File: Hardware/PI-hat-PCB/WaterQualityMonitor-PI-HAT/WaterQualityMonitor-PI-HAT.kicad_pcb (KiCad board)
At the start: 2 copper layers, 65 x 106.7 mm, 84 parts, among them IC1 P82B96TD,118, IC2 DMMT5401-7-F, J1 Screw_Terminal_01x04, J10 GPIO, J2 Screw_Terminal_01x04, J3 Screw_Terminal_01x04, J4 Screw_Terminal_01x02, J5 Jack-DC 12V+, J6 SM04B-SRSS-TB(LF)(SN), M1 Fan, Q1 IRL540SPBF, Q2 IRL540SPBF, Q3 DMG2305UX-7, U1 DRV8870DDA, U2 TPS61169DCKR, U3 TMC2208_SILENTSTEPSTICK, U4 TMC2208_SILENTSTEPSTICK, U5 RT7272AGSP, U6 TMC2208_SILENTSTEPSTICK, U7 DRV8838, U8 RT7272AGSP, U9 CAT24C256

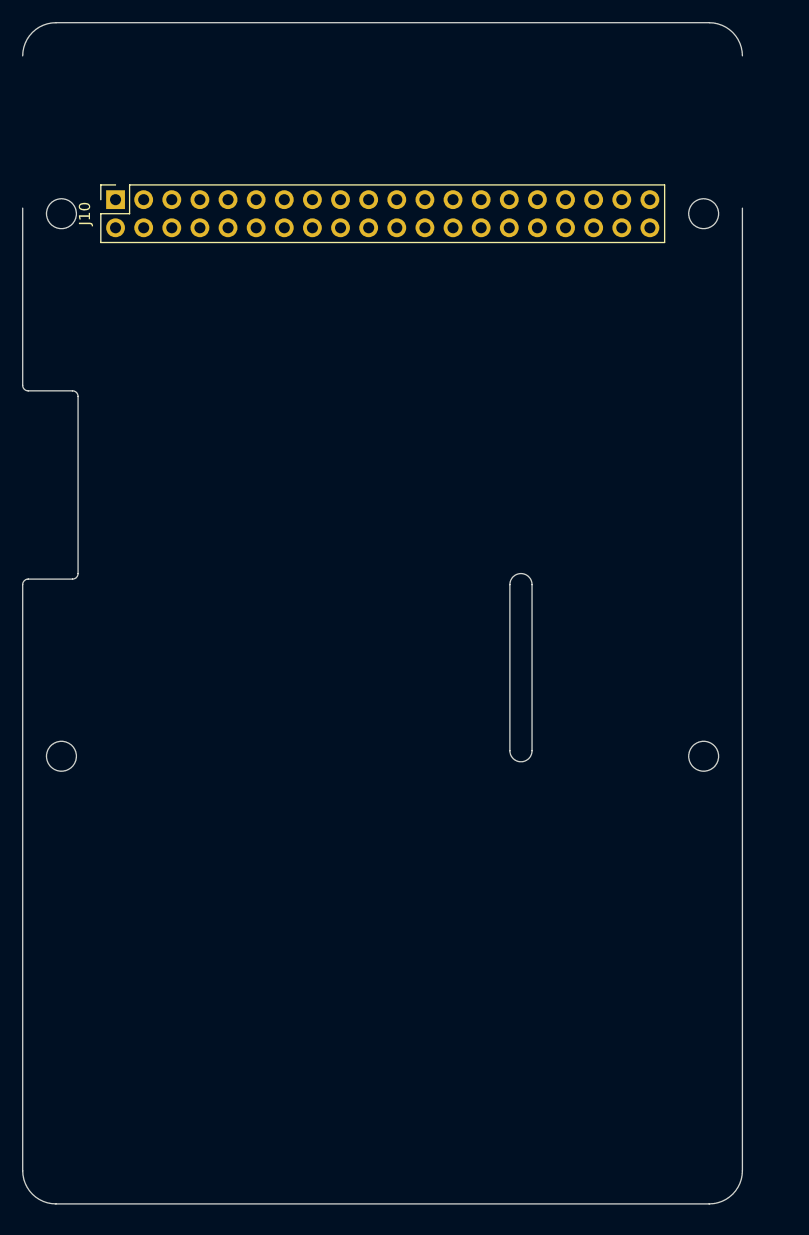
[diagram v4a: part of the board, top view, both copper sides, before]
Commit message: removed board outline
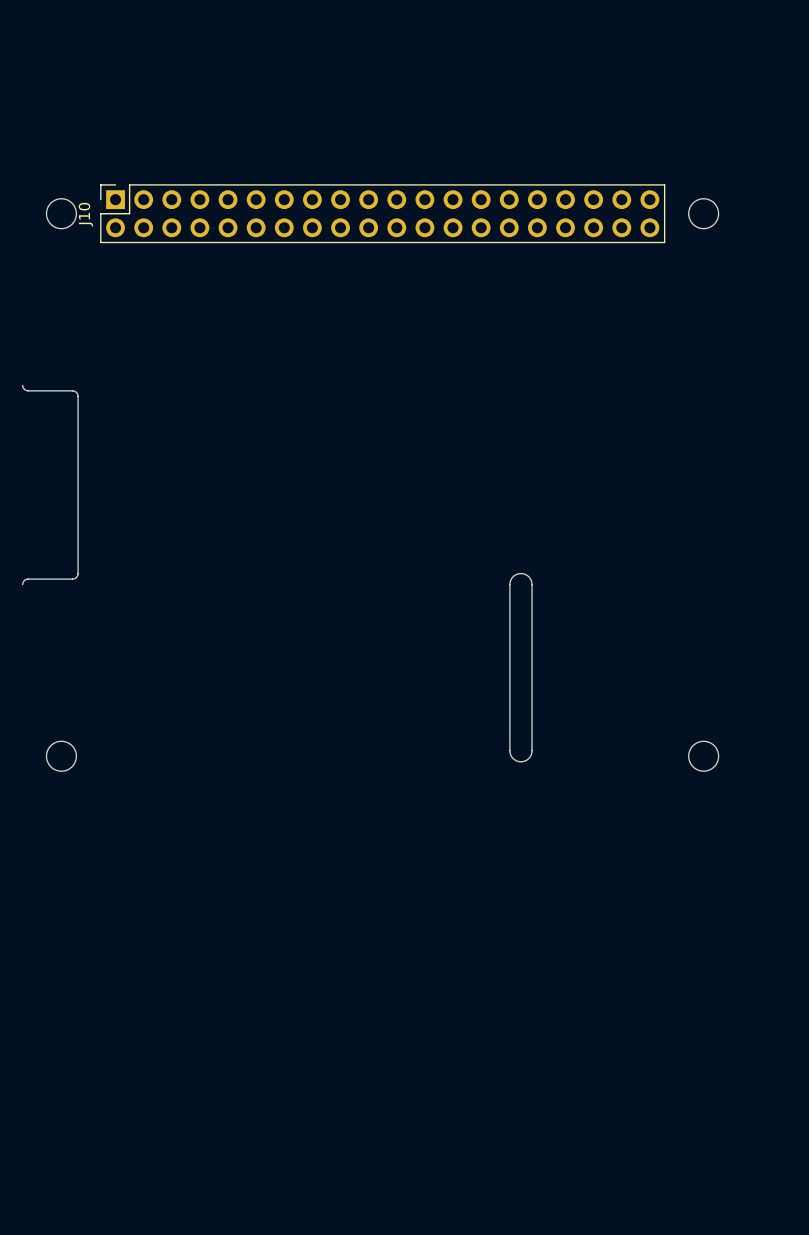
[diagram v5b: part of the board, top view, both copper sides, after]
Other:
- board size 65 x 106.7 mm -> 46 x 34 mm
- board text added: "CAMERÀ"
- board text removed: "CAMERA (OPTIONAL)"
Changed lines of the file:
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@@
   )
   (gr_rect (start 154.19 171.895) (end 175.19 187.745) (layer "Dwgs.User") (width 0.1) (fill none))
-  (gr_line (start 153.19 137.07) (end 153.19 123.3172) (layer "Dwgs.User") (width 0.1))
   (gr_rect (start 175.19 154.52) (end 158.09 167.62) (layer "Dwgs.User") (width 0.1) (fill none))
-  (gr_line (start 88.19 137.0192) (end 88.189 123.3172) (layer "Dwgs.User") (width 0.1))
   (gr_rect (start 175.19 136.425925) (end 158.09 149.525925) (layer "Dwgs.User") (width 0.1) (fill none))
   (gr_arc (start 88.69 153.57) (mid 88.336447 153.423553) (end 88.19 153.07) (layer "Edge.Cuts") (width 0.1))
-  (gr_arc (start 150.19 120.32) (mid 152.31132 121.19868) (end 153.19 123.32) (layer "Edge.Cuts") (width 0.1))
-  (gr_line (start 153.19 224) (end 153.19 137.07) (layer "Edge.Cuts") (width 0.1))
-  (gr_line (start 88.19 137.07) (end 88.19 153.07) (layer "Edge.Cuts") (width 0.1))
   (gr_line (start 134.19 171.07) (end 134.19 186.07) (layer "Edge.Cuts") (width 0.1))
   (gr_line (start 132.19 186.07) (end 132.19 171.07) (layer "Edge.Cuts") (width 0.1))
-  (gr_arc (start 91.19 227) (mid 89.06868 226.12132) (end 88.19 224) (layer "Edge.Cuts") (width 0.1))
-  (gr_line (start 91.19 227) (end 150.19 227) (layer "Edge.Cuts") (width 0.1))
   (gr_line (start 92.69 170.57) (end 88.69 170.57) (layer "Edge.Cuts") (width 0.1))
   (gr_arc (start 132.19 171.07) (mid 133.19 170.07) (end 134.19 171.07) (layer "Edge.Cuts") (width 0.1))
   (gr_arc (start 88.19 171.07) (mid 88.336138 170.716755) (end 88.689127 170.570001) (layer "Edge.Cuts") (width 0.1))
-  (gr_arc (start 153.19 224) (mid 152.31132 226.12132) (end 150.19 227) (layer "Edge.Cuts") (width 0.1))
   (gr_line (start 93.19 154.07) (end 93.19 170.07) (layer "Edge.Cuts") (width 0.1))
-  (gr_arc (start 88.19 123.32) (mid 89.06868 121.19868) (end 91.19 120.32) (layer "Edge.Cuts") (width 0.1))
   (gr_arc (start 134.19 186.07) (mid 133.19 187.07) (end 132.19 186.07) (layer "Edge.Cuts") (width 0.1))
-  (gr_line (start 88.19 171.07) (end 88.19 224) (layer "Edge.Cuts") (width 0.1))
   (gr_line (start 88.69 153.57) (end 92.69 153.57) (layer "Edge.Cuts") (width 0.1))
   (gr_arc (start 93.19 170.07) (mid 93.043553 170.423553) (end 92.69 170.57) (layer "Edge.Cuts") (width 0.1))
   (gr_arc (start 92.69 153.57) (mid 93.043553 153.716447) (end 93.19 154.07) (layer "Edge.Cuts") (width 0.1))
-  (gr_line (start 150.19 120.32) (end 91.19 120.32) (layer "Edge.Cuts") (width 0.1))
   (gr_text "USB" (at 165.914 161.622) (layer "Dwgs.User")
     (effects (font (size 2 2) (thickness 0.15)))
@@
     (effects (font (size 1 1) (thickness 0.15)))
   )
-  (gr_text "CAMERA (OPTIONAL)" (at 133.19 178.57 90) (layer "Dwgs.User")
+  (gr_text "CAMERÀ" (at 133.19 178.57 90) (layer "Dwgs.User")
     (effects (font (size 1 1) (thickness 0.15)))
   )

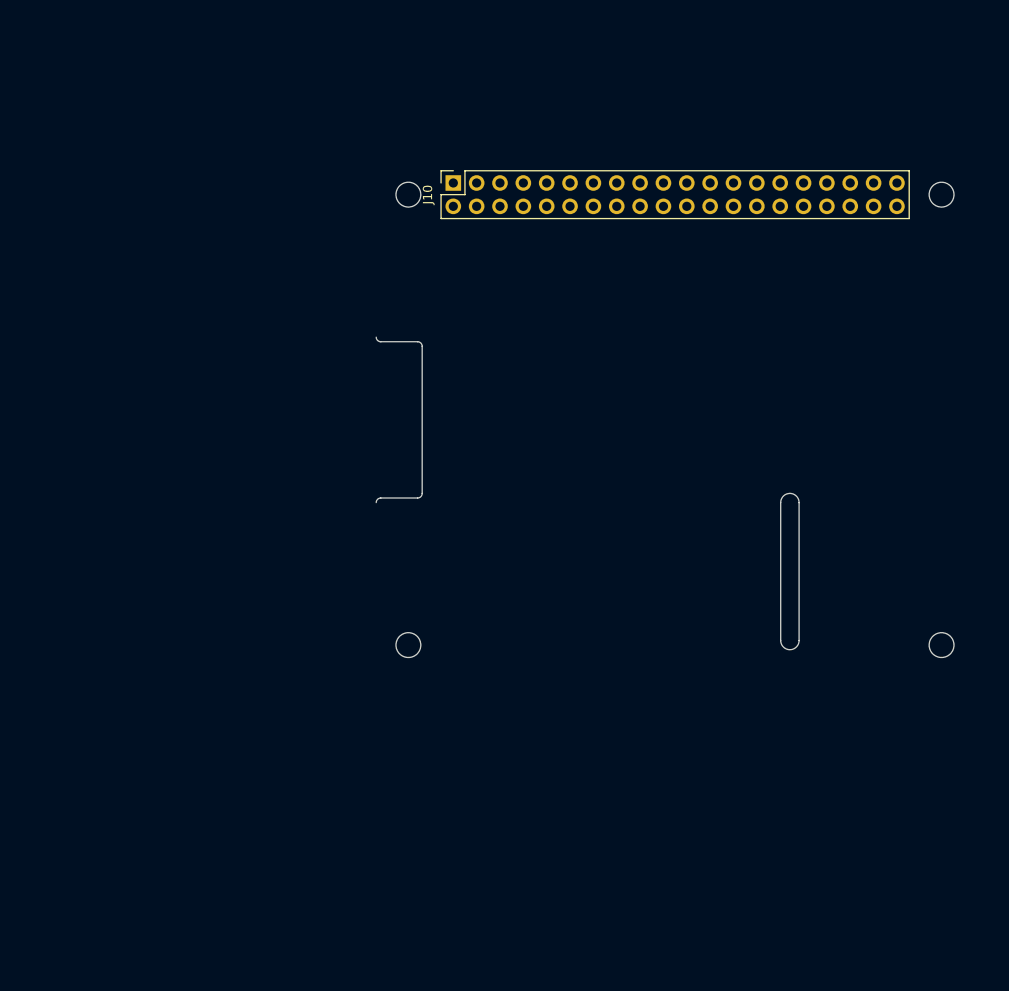
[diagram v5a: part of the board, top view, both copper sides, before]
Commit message: Updated PCB outline again
left power, hdmi and microphone ports free
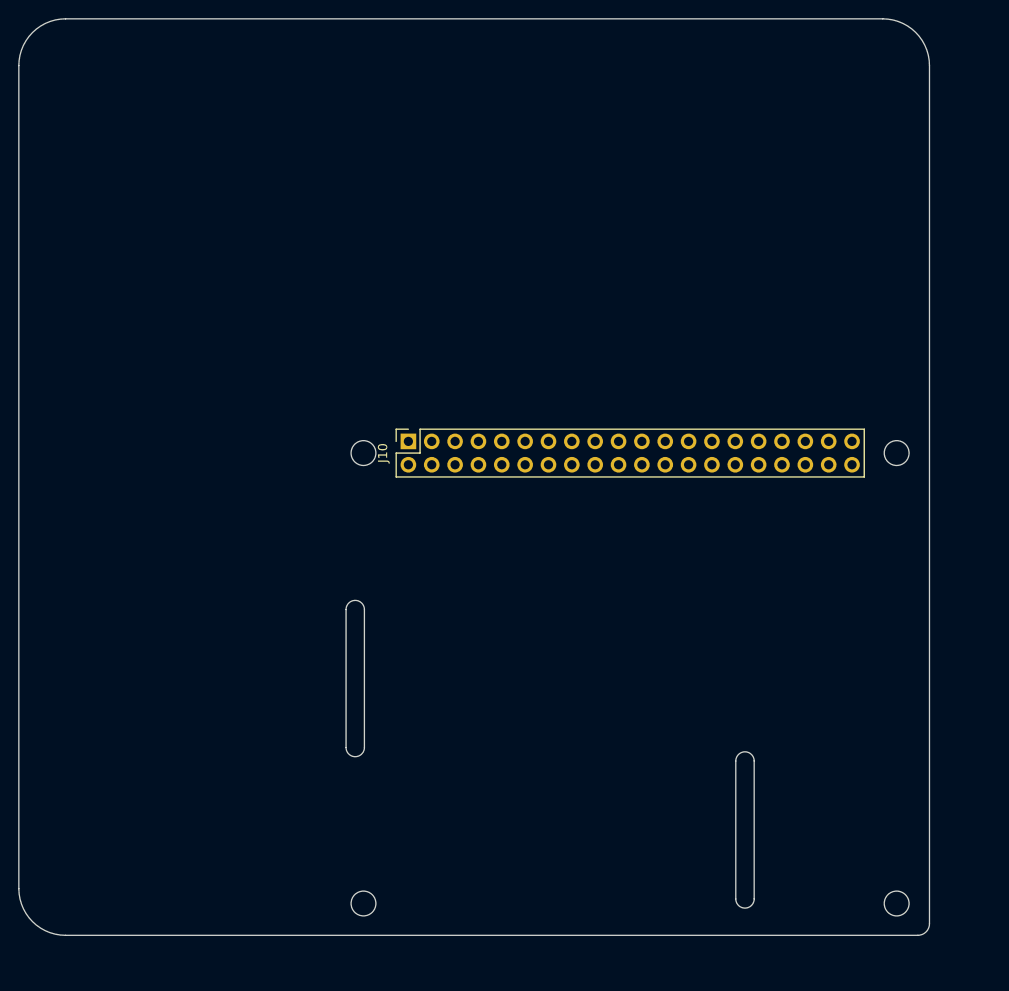
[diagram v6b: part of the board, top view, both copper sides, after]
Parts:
- moved J10 28.5 mm to (91.7, 164.4)
- moved MH1 28.5 mm to (86.8, 165.7)
- moved MH2 28.5 mm to (144.8, 165.7)
- moved MH3 28.5 mm to (86.8, 214.7)
- moved MH4 28.5 mm to (144.8, 214.7)
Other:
- board size 46 x 34 mm -> 99.1 x 99.7 mm
- board text added: "DISPLAY"
- board text removed: "DISPLAY (OPTIONAL)"
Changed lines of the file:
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@@
   )
   (footprint "MountingHole:MountingHole_2.7mm_M2.5" (layer "F.Cu")
-    (at 149.69 137.57)
+    (at 144.805 165.68)
     (descr "Mounting Hole 2.7mm, no annular, M2.5")
     (tags "mounting hole 2.7mm no annular m2.5")
@@
   )
   (footprint "Connector_PinSocket_2.54mm:PinSocket_2x20_P2.54mm_Vertical" (layer "F.Cu")
-    (at 96.5756 136.302 90)
+    (at 91.6906 164.412 90)
     (descr "Through hole straight socket strip, 2x20, 2.54mm pitch, double cols (from Kicad 4.0.7), script generated")
     (tags "Through hole socket strip THT 2x20 2.54mm double row")
@@
   )
   (footprint "MountingHole:MountingHole_2.7mm_M2.5" (layer "F.Cu")
-    (at 91.69 186.57)
+    (at 86.805 214.68)
     (descr "Mounting Hole 2.7mm, no annular, M2.5")
     (tags "mounting hole 2.7mm no annular m2.5")
@@
   )
   (footprint "MountingHole:MountingHole_2.7mm_M2.5" (layer "F.Cu")
-    (at 91.69 137.57)
+    (at 86.805 165.68)
     (descr "Mounting Hole 2.7mm, no annular, M2.5")
     (tags "mounting hole 2.7mm no annular m2.5")
@@
   )
   (footprint "MountingHole:MountingHole_2.7mm_M2.5" (layer "F.Cu")
-    (at 149.69 186.57)
+    (at 144.805 214.68)
     (descr "Mounting Hole 2.7mm, no annular, M2.5")
     (tags "mounting hole 2.7mm no annular m2.5")
@@
     )
   )
-  (gr_rect (start 154.19 171.895) (end 175.19 187.745) (layer "Dwgs.User") (width 0.1) (fill none))
-  (gr_rect (start 175.19 154.52) (end 158.09 167.62) (layer "Dwgs.User") (width 0.1) (fill none))
-  (gr_rect (start 175.19 136.425925) (end 158.09 149.525925) (layer "Dwgs.User") (width 0.1) (fill none))
-  (gr_arc (start 88.69 153.57) (mid 88.336447 153.423553) (end 88.19 153.07) (layer "Edge.Cuts") (width 0.1))
-  (gr_line (start 134.19 171.07) (end 134.19 186.07) (layer "Edge.Cuts") (width 0.1))
-  (gr_line (start 132.19 186.07) (end 132.19 171.07) (layer "Edge.Cuts") (width 0.1))
-  (gr_line (start 92.69 170.57) (end 88.69 170.57) (layer "Edge.Cuts") (width 0.1))
-  (gr_arc (start 132.19 171.07) (mid 133.19 170.07) (end 134.19 171.07) (layer "Edge.Cuts") (width 0.1))
-  (gr_arc (start 88.19 171.07) (mid 88.336138 170.716755) (end 88.689127 170.570001) (layer "Edge.Cuts") (width 0.1))
-  (gr_line (start 93.19 154.07) (end 93.19 170.07) (layer "Edge.Cuts") (width 0.1))
-  (gr_arc (start 134.19 186.07) (mid 133.19 187.07) (end 132.19 186.07) (layer "Edge.Cuts") (width 0.1))
-  (gr_line (start 88.69 153.57) (end 92.69 153.57) (layer "Edge.Cuts") (width 0.1))
-  (gr_arc (start 93.19 170.07) (mid 93.043553 170.423553) (end 92.69 170.57) (layer "Edge.Cuts") (width 0.1))
-  (gr_arc (start 92.69 153.57) (mid 93.043553 153.716447) (end 93.19 154.07) (layer "Edge.Cuts") (width 0.1))
-  (gr_text "USB" (at 165.914 161.622) (layer "Dwgs.User")
+  (gr_rect (start 149.305 200.005) (end 170.305 215.855) (layer "Dwgs.User") (width 0.1) (fill none))
+  (gr_rect (start 170.305 182.63) (end 153.205 195.73) (layer "Dwgs.User") (width 0.1) (fill none))
+  (gr_rect (start 170.305 164.535925) (end 153.205 177.635925) (layer "Dwgs.User") (width 0.1) (fill none))
+  (gr_line (start 86.907 182.708) (end 86.907 197.708) (layer "Edge.Cuts") (width 0.1))
+  (gr_line (start 49.315 213.061) (end 49.315 123.526) (layer "Edge.Cuts") (width 0.1))
+  (gr_line (start 147.105 218.141) (end 54.395 218.141) (layer "Edge.Cuts") (width 0.1))
+  (gr_arc (start 84.907 182.708) (mid 85.907 181.708) (end 86.907 182.708) (layer "Edge.Cuts") (width 0.1))
+  (gr_line (start 148.375002 123.525998) (end 148.375002 216.871) (layer "Edge.Cuts") (width 0.1))
+  (gr_arc (start 143.295002 118.445998) (mid 146.887104 119.933896) (end 148.375002 123.525998) (layer "Edge.Cuts") (width 0.1))
+  (gr_line (start 84.907 197.708) (end 84.907 182.708) (layer "Edge.Cuts") (width 0.1))
+  (gr_line (start 54.395 118.446) (end 143.295002 118.446) (layer "Edge.Cuts") (width 0.1))
+  (gr_line (start 129.305 199.18) (end 129.305 214.18) (layer "Edge.Cuts") (width 0.1))
+  (gr_line (start 127.305 214.18) (end 127.305 199.18) (layer "Edge.Cuts") (width 0.1))
+  (gr_arc (start 148.375 216.871) (mid 148.003026 217.769026) (end 147.105 218.141) (layer "Edge.Cuts") (width 0.1))
+  (gr_arc (start 54.395 218.141) (mid 50.802898 216.653102) (end 49.315 213.061) (layer "Edge.Cuts") (width 0.1))
+  (gr_arc (start 127.305 199.18) (mid 128.305 198.18) (end 129.305 199.18) (layer "Edge.Cuts") (width 0.1))
+  (gr_arc (start 49.315 123.526) (mid 50.802898 119.933898) (end 54.395 118.446) (layer "Edge.Cuts") (width 0.1))
+  (gr_arc (start 129.305 214.18) (mid 128.305 215.18) (end 127.305 214.18) (layer "Edge.Cuts") (width 0.1))
+  (gr_arc (start 86.907 197.708) (mid 85.907 198.708) (end 84.907 197.708) (layer "Edge.Cuts") (width 0.1))
+  (gr_text "USB" (at 161.029 189.732) (layer "Dwgs.User")
     (effects (font (size 2 2) (thickness 0.15)))
   )
-  (gr_text "RJ45" (at 164.39 179.91) (layer "Dwgs.User")
+  (gr_text "RJ45" (at 159.505 208.02) (layer "Dwgs.User")
     (effects (font (size 2 2) (thickness 0.15)))
   )
-  (gr_text "DISPLAY (OPTIONAL)" (at 90.69 162.07 90) (layer "Dwgs.User")
+  (gr_text "DISPLAY" (at 85.891 190.208 90) (layer "Dwgs.User")
     (effects (font (size 1 1) (thickness 0.15)))
   )
-  (gr_text "CAMERÀ" (at 133.19 178.57 90) (layer "Dwgs.User")
+  (gr_text "CAMERÀ" (at 128.305 206.68 90) (layer "Dwgs.User")
     (effects (font (size 1 1) (thickness 0.15)))
   )
-  (gr_text "USB" (at 166.422 142.318) (layer "Dwgs.User")
+  (gr_text "USB" (at 161.537 170.428) (layer "Dwgs.User")
     (effects (font (size 2 2) (thickness 0.15)))
   )
-  (gr_text "PoE" (at 149.69 143.71) (layer "Dwgs.User")
+  (gr_text "PoE" (at 144.805 171.82) (layer "Dwgs.User")
     (effects (font (size 1 1) (thickness 0.15)))
   )
@@
     (polygon
       (pts
-        (xy 152.19 146.21)
-        (xy 147.19 146.21)
-        (xy 147.19 141.21)
-        (xy 152.19 141.21)
+        (xy 147.305 174.32)
+        (xy 142.305 174.32)
+        (xy 142.305 169.32)
+        (xy 147.305 169.32)
       )
     )
   )
+  (group "" (id 7e2a50c6-4801-4c85-9f0a-4a59d730581f)
+    (members
+      00000000-0000-0000-0000-0000580cbbff
+      06809ba2-f11a-40ba-a772-c51d31060648
+      28264392-6120-4837-998c-85a4116c5c9c
+      6a8fdcbc-fafe-4112-8389-467d0507544d
+      f6076878-26ce-4071-b56f-bc040c8baf64
+    )
+  )
+  (group "" (id 83ed5d0b-8fbe-4b0c-82e6-92d3041e5b57)
+    (members
+      00000000-0000-0000-0000-0000580cbbe9
+      00000000-0000-0000-0000-0000580cbbeb
+      0361f1e7-3200-462a-a139-1890cc8ecc5d
+      0beff73c-ea66-46e4-96f9-c0c7195d2160
+      1130f673-5a87-4c35-9d4e-610acc21fffd
+      2429cb60-a9f1-4ae8-8b94-44df70f8227f
+      29df31ed-bd0f-485f-bd0e-edc97e11b54b
+      32a6c0db-7669-439c-bf73-71577c4282a3
+      38532103-80f2-46ad-86ce-93eab10ab2a2
+      3b108586-2520-4867-9c38-7334a1000bb5
+      4ca5af88-2017-47d4-83fb-2067754a83f2
+      55c2b75d-5e45-4a08-ab83-0bcdd5f03b6a
+      6528a76f-b7a7-4621-952f-d7da1058963a
+      728bdf39-b274-4d82-88b8-c1bd9ff8ead6
+      7e2a50c6-4801-4c85-9f0a-4a59d730581f
+      7e8d827e-a7ed-44d4-95fc-a91af7cef820
+      89efe179-e83b-40db-abd4-3fc7739e57ac
+      ab1c4aff-2e3b-49c6-ac2a-6145f3d7130f
+      ad629bd4-e7e1-40e2-81d6-711e1f1d1fae
+      af1f744a-3b0b-40fd-a2e7-93eba615b41c
+      b1d14817-fd88-44a9-b8e9-574b3194c17b
+      c5d6c104-5680-4140-a821-8340078f5018
+      d231d6dd-8c0c-4ff1-9cd6-f8ed758e2643
+    )
+  )

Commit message: added 2 GPIO power pins (high loads)
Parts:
- added F5: 3.2A, Fuse:Fuse_1206_3216Metric_Pad1.42x1.75mm_HandSolder, F.Cu at (314.5, 67.5)
- added F6: 3.2A, Fuse:Fuse_1206_3216Metric_Pad1.42x1.75mm_HandSolder, F.Cu at (342.7, 46.3)
- added J7: Screw_Terminal_01x02, TerminalBlock:TerminalBlock_Altech_AK300-2_P5.00mm, F.Cu at (324.8, 31.1)
- added J8: Screw_Terminal_01x02, TerminalBlock:TerminalBlock_Altech_AK300-2_P5.00mm, F.Cu at (324.8, 45.1)
- added Q4: IRL540SPBF, SmacSYs:IRL540SPBF, F.Cu at (283.9, 59.6)
- added Q5: IRL540SPBF, SmacSYs:IRL540SPBF, F.Cu at (314.6, 25.6)
- J1: moved to F.Cu
- moved R13 263.4 mm to (378.4, 40.8)
- moved C19 262.3 mm to (376.8, 37.4)
- moved C20 241.5 mm to (382.8, 34.1)
- moved R16 240.4 mm to (382.8, 37.4)
- moved R14 234.9 mm to (363.2, 53.2)
- moved R17 234.9 mm to (372.4, 44.2)
- moved C16 234.9 mm to (372.4, 40.9)
- moved C17 234.9 mm to (357.3, 49.9)
- moved C18 234.9 mm to (357.3, 53.3)
- moved C21 234.9 mm to (376.8, 34.1)
- moved C22 234.9 mm to (366.4, 43.5)
- moved C23 234.9 mm to (363.3, 49.9)
- moved C24 234.9 mm to (370.7, 37.5)
- moved L3 234.9 mm to (370.8, 34.1)
- moved PS1 234.9 mm to (358.6, 38.8)
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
